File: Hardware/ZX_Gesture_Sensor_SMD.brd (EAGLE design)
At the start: 61.8 x 16.5 mm, 50 parts, among them Q1 MMBT2222A, Q2 MOSFET-NCHANNEL2N7002PW, U1 PIC16F1823-14PINTSSOP, U2 MCP6021T-E/OT, U3 DMC2700UDM, U4 DMC2700UDM, U5 TSSP57038

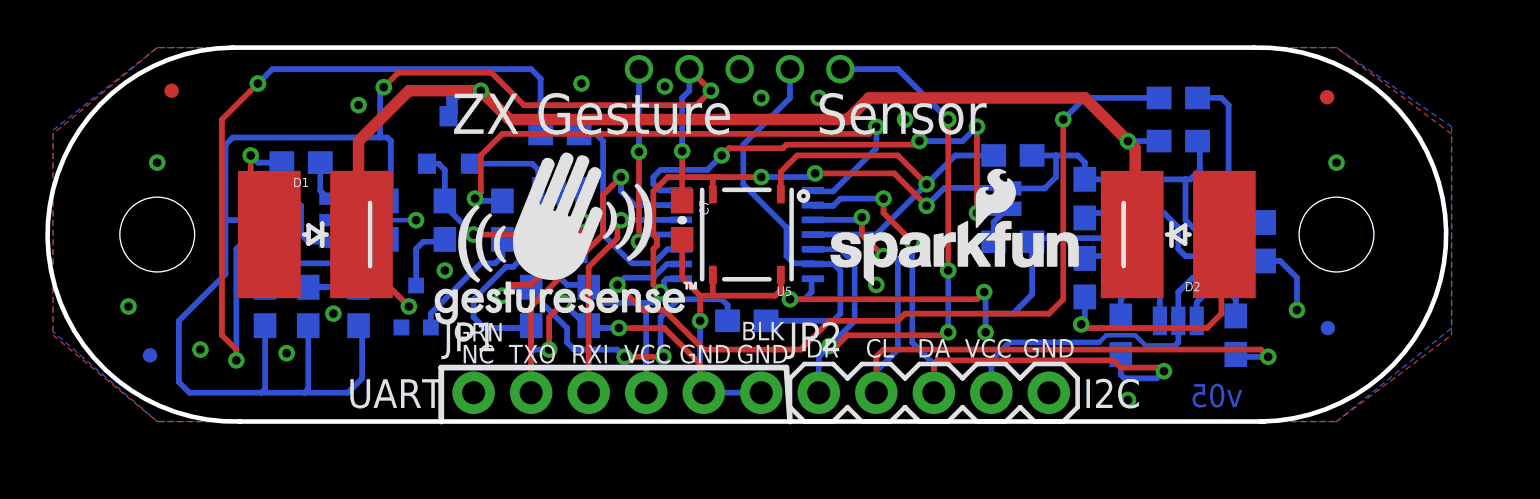
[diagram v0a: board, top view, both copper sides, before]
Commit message: Updated BRD and SCH Files per Design Review
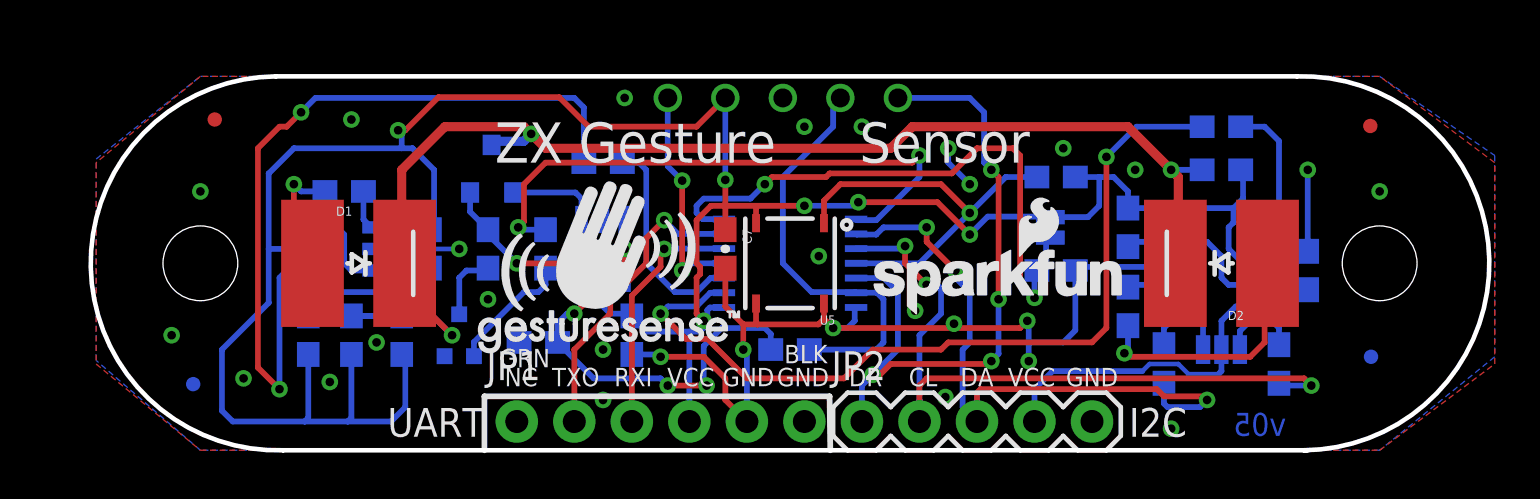
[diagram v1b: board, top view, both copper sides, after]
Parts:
- moved TP5 2.84 mm to (35.2, 15.6)
- moved TP4 2.56 mm to (32.7, 15.6)
- moved R13 2.29 mm to (22.2, 12.7)
- moved R7 2.29 mm to (45.4, 9.84)
- moved SJ2 2.29 mm to (42.0, 9.84)
- moved TP3 2.29 mm to (30.2, 15.6)
- moved C1 2.29 mm to (13.3, 5.08)
- moved C3 2.29 mm to (11.1, 5.08)
- moved C5 2.29 mm to (53.3, 7.94)
- moved C6 2.29 mm to (49.5, 12.4)
- moved C8 2.29 mm to (23.5, 5.08)
- moved D2 2.29 mm to (49.5, 8.26)
- moved FID2 2.29 mm to (56.1, 4.13)
- moved FID4 2.29 mm to (56.1, 14.3)
- moved JP2 2.29 mm to (33.7, 1.27)
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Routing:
- net GND: track 72.1 -> 51.7 mm, vias 25 -> 29
- net I2C_ADDR: track 23.8 -> 26.6 mm, vias 4 -> 2
- net VCC: track 137.4 -> 140.0 mm
- net I2C_SDA: track 27.4 -> 29.4 mm
- net N$1: track 21.5 -> 20.1 mm
- net UART_RX: track 14.7 -> 13.4 mm
- net I2C_SCL: track 31.9 -> 32.9 mm
- net ICSPDAT/DACOUT: track 17.9 -> 18.8 mm
- net COMMON: track 61.5 -> 60.8 mm

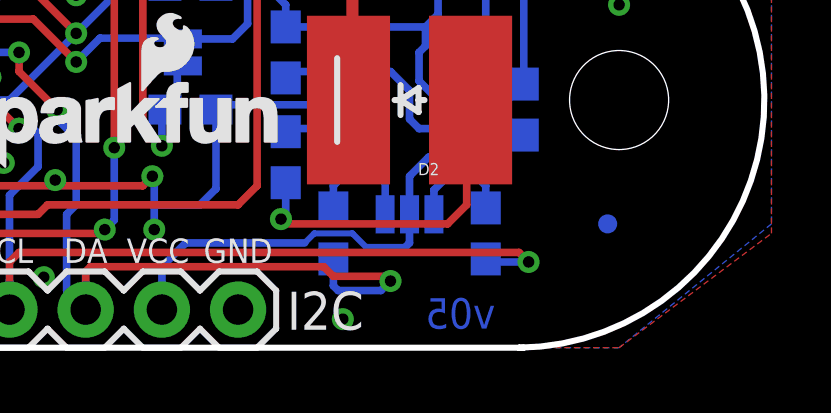
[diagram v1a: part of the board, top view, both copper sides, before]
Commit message: -Updated v05 to v10 -moved back silk labels -all copper is unchanged from v05.
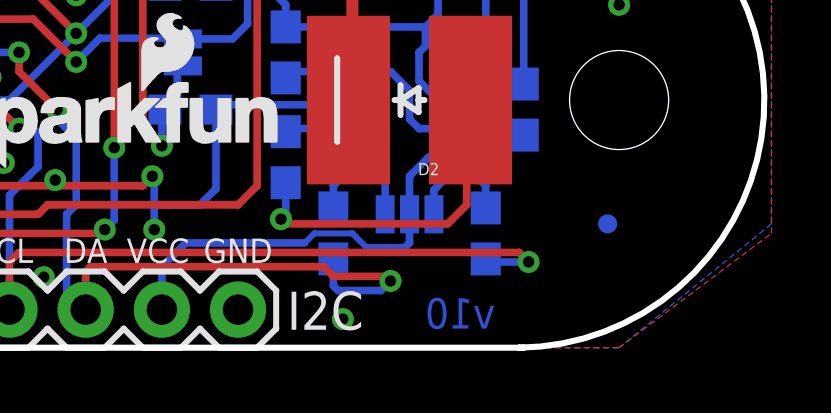
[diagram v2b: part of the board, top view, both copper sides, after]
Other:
- board text added: "v10"
- board text removed: "v05"
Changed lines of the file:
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@@
 <text x="16.97355" y="1.2319" size="1.27" layer="21" font="vector" ratio="15" align="center-right">UART</text>
 <text x="45.44695" y="1.2319" size="1.27" layer="21" font="vector" ratio="15" align="center-left">I2C</text>
-<text x="44.1325" y="9.68375" size="0.8128" layer="22" font="vector" ratio="15" rot="MR270" align="bottom-center">I2C Addr</text>
+<text x="44.6405" y="9.93775" size="0.8128" layer="22" font="vector" ratio="15" rot="MR270" align="bottom-center">I2C Addr</text>
 <text x="23.65375" y="12.7" size="1.778" layer="21" font="vector" ratio="15" align="bottom-center">ZX Gesture</text>
 <text x="48.9585" y="5.715" size="0.8128" layer="22" font="vector" ratio="15" rot="MR0" align="bottom-center">I2C Pullups</text>
@@
 <text x="38.608" y="2.3495" size="0.8128" layer="22" font="vector" ratio="15" rot="MR0" align="bottom-center">DA</text>
 <text x="25.5905" y="-15.494" size="1.778" layer="51" font="vector">Mary West </text>
-<text x="30.28315" y="13.462" size="1.016" layer="22" font="vector" ratio="15" rot="MR0" align="bottom-center">ZX Gesture</text>
-<text x="22.0599" y="13.3985" size="1.016" layer="22" font="vector" ratio="15" rot="MR0" align="bottom-center">Sensor</text>
+<text x="32.18815" y="13.462" size="1.016" layer="22" font="vector" ratio="15" rot="MR0" align="bottom-center">ZX Gesture</text>
+<text x="24.3459" y="13.5255" size="1.016" layer="22" font="vector" ratio="15" rot="MR0" align="bottom-center">Sensor</text>
 <text x="12.14755" y="1.26365" size="1.27" layer="22" font="vector" ratio="15" rot="MR0" align="center-right">UART</text>
 <text x="48.05045" y="1.39065" size="1.27" layer="22" font="vector" ratio="15" rot="MR0" align="center-left">I2C</text>
@@
 <wire x1="8.09625" y1="0" x2="53.18125" y2="0" width="0.2032" layer="20"/>
 <wire x1="53.18125" y1="0" x2="53.34" y2="0" width="0.2032" layer="20"/>
-<text x="52.3875" y="0.635" size="1.016" layer="16" ratio="20" rot="MR0">v05</text>
+<text x="52.3875" y="0.635" size="1.016" layer="16" ratio="20" rot="MR0">v10</text>
 <wire x1="52.86375" y1="16.51" x2="7.77875" y2="16.51" width="0.2032" layer="20"/>
 <wire x1="8.09625" y1="0" x2="7.77875" y2="16.51" width="0.2032" layer="20" curve="-181.090425"/>
